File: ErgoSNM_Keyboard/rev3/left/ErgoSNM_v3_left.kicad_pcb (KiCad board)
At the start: 2 copper layers, 115.6 x 106.7 mm, 89 parts, among them J1 USB_C_Receptacle_USB2.0, J2 Conn_01x04, J3 Conn_01x02, J4 Conn_01x08, SW1 SW_DPDT_x2, SW3 RESET, U1 RT9013-33GB, U2 E73-2G4M08S1C, U4 TPS61220DCK, Y1 32.768kHz

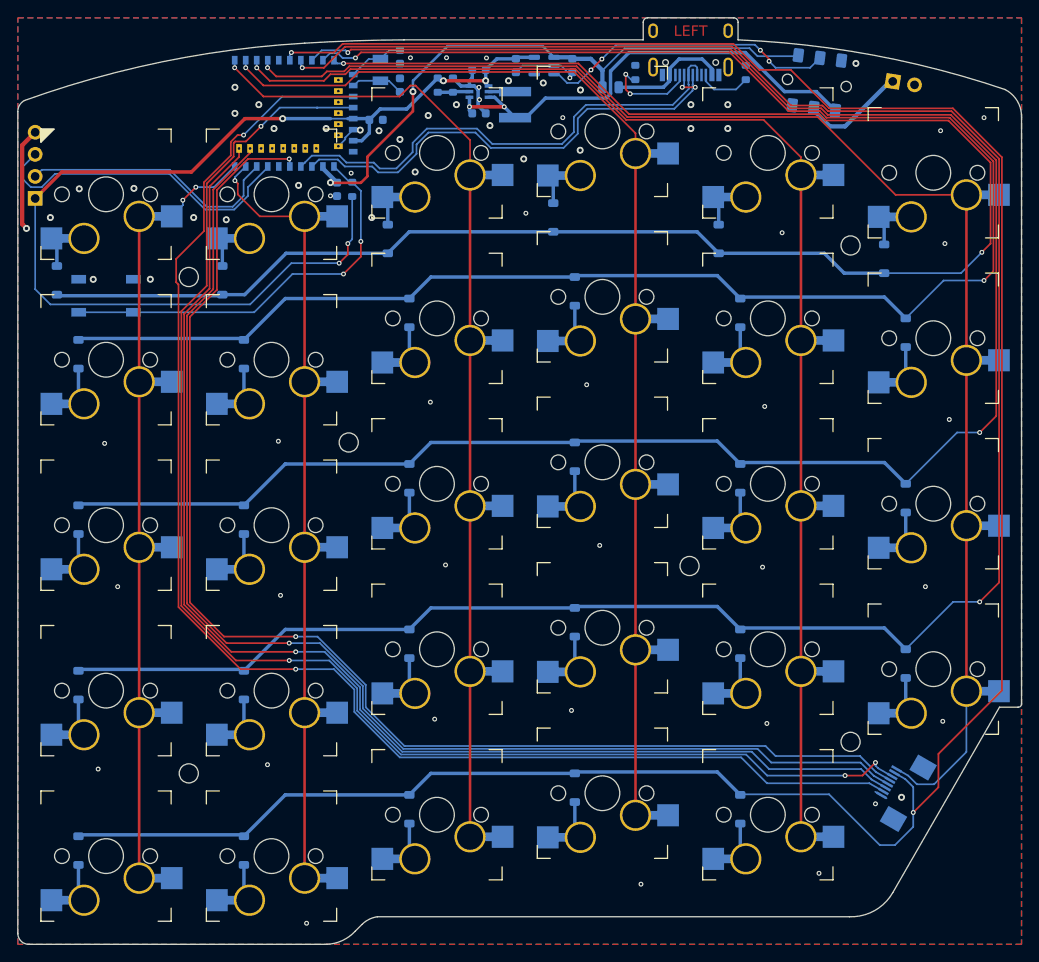
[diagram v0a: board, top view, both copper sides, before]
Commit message: Add key-matrix test pointes (2.54mm pin header)
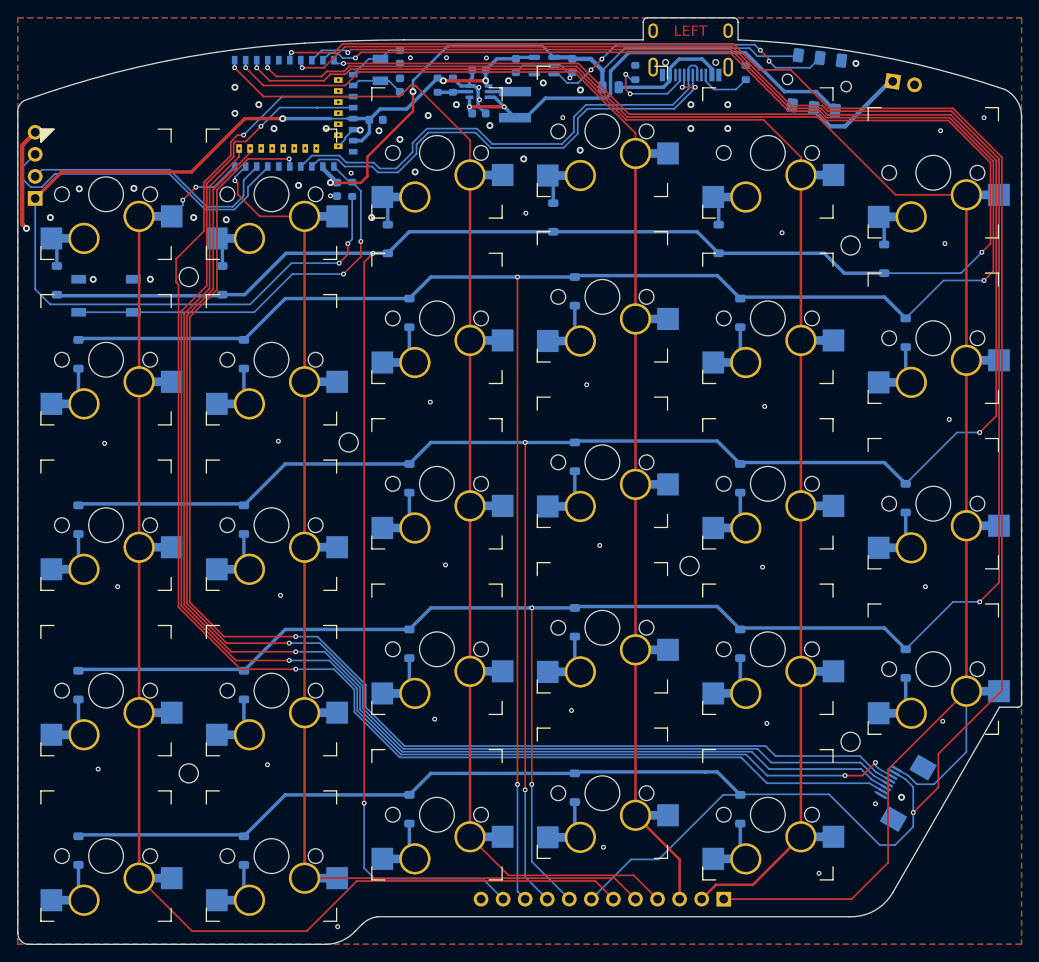
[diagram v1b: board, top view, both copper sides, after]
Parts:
- added J5: Conn_01x12, Connector_PinHeader_2.54mm:PinHeader_1x12_P2.54mm_Vertical, B.Cu at (142.2, 126.9)
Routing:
- net ROW_0: track 203.8 -> 292.5 mm, vias 2 -> 4
- net ROW_1: track 208.8 -> 280.8 mm, vias 2 -> 4
- net COL_0: track 86.2 -> 146.6 mm
- net ROW_2: track 228.5 -> 282.2 mm, vias 2 -> 4
- net COL_5: track 162.7 -> 206.8 mm
- net COL_1: track 88.8 -> 127.9 mm
- net ROW_3: track 250.9 -> 286.2 mm, vias 2 -> 4
- net COL_2: track 112.7 -> 137.2 mm
- net ROW_4: track 279.4 -> 301.5 mm
- net COL_4: track 147.2 -> 161.6 mm
- net COL_3: track 128.7 -> 140.4 mm

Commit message: Update submodule
Update submodule

Update switch footprint
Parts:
- KEY1: footprint key-switches:MX_switch_PTH_hotswap_A -> key-switches:SW_MX_HotSwap_PTH
- KEY10: renamed from KEY26; footprint key-switches:MX_switch_PTH_hotswap_A -> key-switches:SW_MX_HotSwap_PTH
- KEY11: renamed from KEY3; footprint key-switches:MX_switch_PTH_hotswap_A -> key-switches:SW_MX_HotSwap_PTH
- KEY12: renamed from KEY9; footprint key-switches:MX_switch_PTH_hotswap_A -> key-switches:SW_MX_HotSwap_PTH
- KEY13: renamed from KEY15; footprint key-switches:MX_switch_PTH_hotswap_A -> key-switches:SW_MX_HotSwap_PTH
- KEY14: renamed from KEY21; footprint key-switches:MX_switch_PTH_hotswap_A -> key-switches:SW_MX_HotSwap_PTH
- KEY15: renamed from KEY27; footprint key-switches:MX_switch_PTH_hotswap_A -> key-switches:SW_MX_HotSwap_PTH
- KEY16: renamed from KEY4; footprint key-switches:MX_switch_PTH_hotswap_A -> key-switches:SW_MX_HotSwap_PTH
- KEY17: renamed from KEY10; footprint key-switches:MX_switch_PTH_hotswap_A -> key-switches:SW_MX_HotSwap_PTH
- KEY18: renamed from KEY16; footprint key-switches:MX_switch_PTH_hotswap_A -> key-switches:SW_MX_HotSwap_PTH
- KEY19: renamed from KEY22; footprint key-switches:MX_switch_PTH_hotswap_A -> key-switches:SW_MX_HotSwap_PTH
- KEY2: renamed from KEY7; footprint key-switches:MX_switch_PTH_hotswap_A -> key-switches:SW_MX_HotSwap_PTH
- KEY20: renamed from KEY28; footprint key-switches:MX_switch_PTH_hotswap_A -> key-switches:SW_MX_HotSwap_PTH
- KEY21: renamed from KEY5; footprint key-switches:MX_switch_PTH_hotswap_A -> key-switches:SW_MX_HotSwap_PTH
- KEY22: renamed from KEY11; footprint key-switches:MX_switch_PTH_hotswap_A -> key-switches:SW_MX_HotSwap_PTH
- KEY23: renamed from KEY17; footprint key-switches:MX_switch_PTH_hotswap_A -> key-switches:SW_MX_HotSwap_PTH
- KEY24: renamed from KEY23; footprint key-switches:MX_switch_PTH_hotswap_A -> key-switches:SW_MX_HotSwap_PTH
- KEY25: renamed from KEY29; footprint key-switches:MX_switch_PTH_hotswap_A -> key-switches:SW_MX_HotSwap_PTH
- KEY26: renamed from KEY6; footprint key-switches:MX_switch_PTH_hotswap_A -> key-switches:SW_MX_HotSwap_PTH
- KEY27: renamed from KEY12; footprint key-switches:MX_switch_PTH_hotswap_A -> key-switches:SW_MX_HotSwap_PTH
- KEY28: renamed from KEY18; footprint key-switches:MX_switch_PTH_hotswap_A -> key-switches:SW_MX_HotSwap_PTH
- KEY29: renamed from KEY24; footprint key-switches:MX_switch_PTH_hotswap_A -> key-switches:SW_MX_HotSwap_PTH
- KEY3: renamed from KEY13; footprint key-switches:MX_switch_PTH_hotswap_A -> key-switches:SW_MX_HotSwap_PTH
- KEY4: renamed from KEY19; footprint key-switches:MX_switch_PTH_hotswap_A -> key-switches:SW_MX_HotSwap_PTH
- KEY5: renamed from KEY25; footprint key-switches:MX_switch_PTH_hotswap_A -> key-switches:SW_MX_HotSwap_PTH
- KEY6: renamed from KEY2; footprint key-switches:MX_switch_PTH_hotswap_A -> key-switches:SW_MX_HotSwap_PTH
- KEY7: renamed from KEY8; footprint key-switches:MX_switch_PTH_hotswap_A -> key-switches:SW_MX_HotSwap_PTH
- KEY8: renamed from KEY14; footprint key-switches:MX_switch_PTH_hotswap_A -> key-switches:SW_MX_HotSwap_PTH
- KEY9: renamed from KEY20; footprint key-switches:MX_switch_PTH_hotswap_A -> key-switches:SW_MX_HotSwap_PTH
- renumbered C5 to C3, C6 to C4, C3 to C5, C4 to C6, D26 to D10, D3 to D11, D9 to D12, D15 to D13, D21 to D14, D27 to D15, D4 to D16, D10 to D17, D16 to D18, D22 to D19, D7 to D2, D28 to D20, D5 to D21, D11 to D22, D17 to D23, D23 to D24, D29 to D25, D6 to D26, D12 to D27, D18 to D28, D24 to D29, D13 to D3, D19 to D4, D25 to D5, D2 to D6, D8 to D7, D14 to D8, D20 to D9, J3 to J2, J2 to J3, SW3 to SW2, U4 to U2, U2 to U3
